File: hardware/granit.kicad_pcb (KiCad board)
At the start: 4 copper layers, 92 x 100 mm, 120 parts, among them J1 USB_C_Receptacle_USB2.0_14P, J2 PCM12SMTR, J3 BM03B-SRSS-TB, J4 SATA_22pin, J5 RJ45_RB1-125B8G1A, J6 12V Screw Terminal, J7 12V Barrel, Q1 2N7002, Q2 FDS4435BZ, Q3 FDS4435BZ, Q4 2N7002, Q5 2N7002, Q6 FDS4435BZ, SW1 SW_Push, U1 USBLC6-2SC6, U2 74AHCT1G125, U3 ASM1061, U4 74AHCT1G32, U5 DS3231MZ, U6 NCP1117-3.3_SOT223, U7 AP64501SP-13, Y1 25MHz

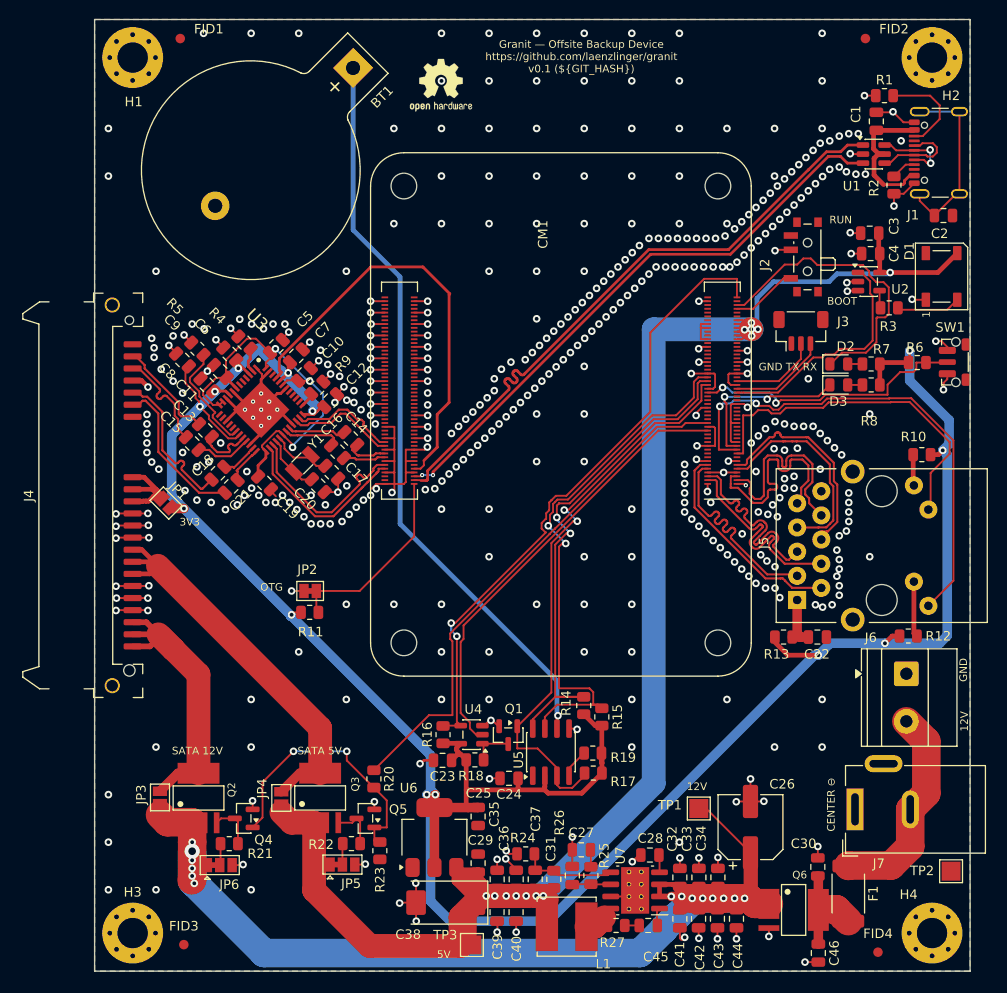
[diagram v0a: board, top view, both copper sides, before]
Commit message: feat: swap RJ45 MagJack to HR911130A (Hanrun GbE)
- New symbol and footprint in granit library
- Pin mapping follows TIA-568B MDI standard
- All 4 Ethernet diff pairs routed with 100Ω impedance
- Pair 1 uses via + bottom trace for length matching
- DRC: 0 violations, 0 unconnected, 0 parity issues
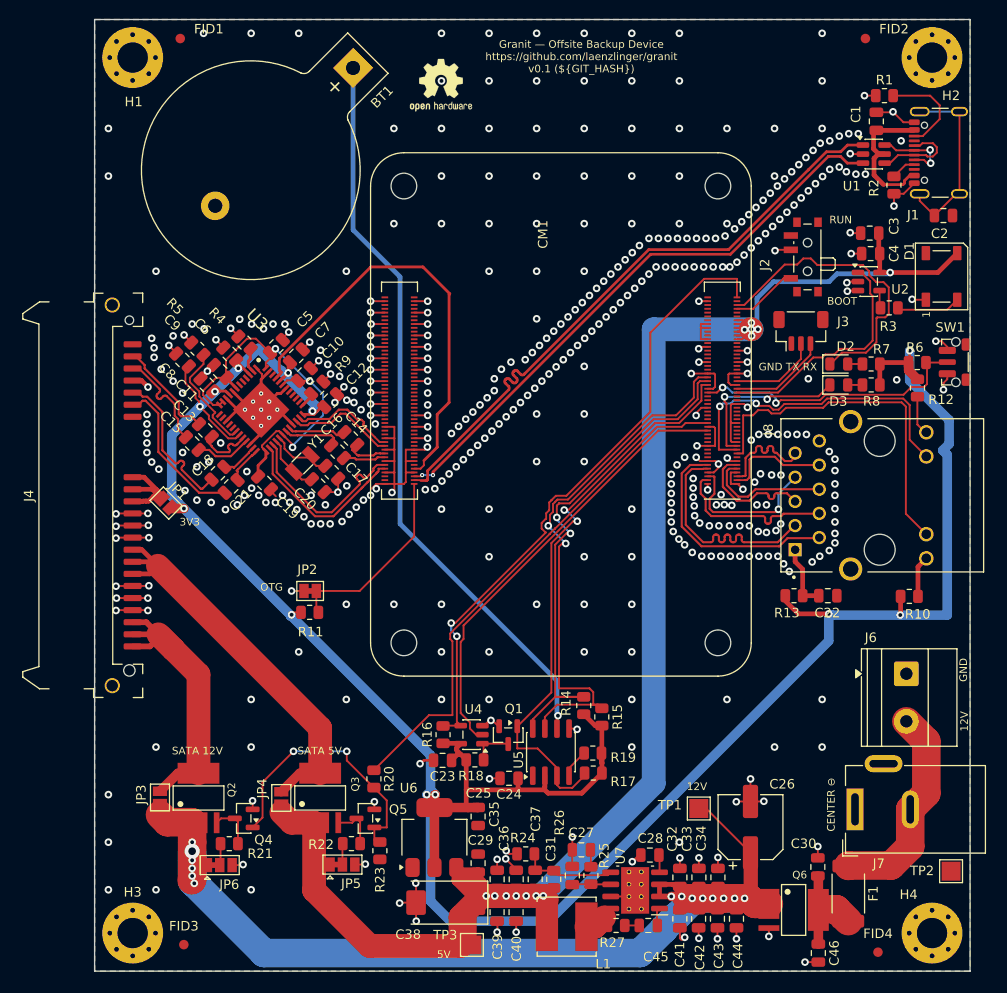
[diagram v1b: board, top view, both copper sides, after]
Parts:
- removed J5: RJ45_RB1-125B8G1A, Connector_RJ:RJ45_UDE_RB1-125B8G1A
- added J8: HR911130A, granit:HANRUN_HR911130A, F.Cu at (102.5, 70.0)
- moved R12 26.1 mm to (106.5, 58.7), turned to -90 degrees
- moved R10 15.0 mm to (105.6, 80.6), turned to 0 degrees
- moved C22 4.48 mm to (97.0, 80.5)
- moved R13 4.48 mm to (93.5, 80.5)
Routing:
- net ETH_nLED1: track 52.5 -> 34.0 mm
- net ETH_P3_N: track 22.2 -> 10.7 mm
- net ETH_P3_P: track 22.3 -> 11.1 mm
- net ETH_P2_P: track 22.6 -> 13.1 mm
- net ETH_P2_N: track 22.3 -> 13.2 mm
- net ETH_P1_N: track 22.2 -> 15.9 mm, vias 0 -> 1
- net ETH_P1_P: track 22.2 -> 17.4 mm
- net Net-(J8-CT_PRI): track 9.85 -> 6.85 mm
- net GND: track 214.3 -> 216.7 mm, vias 450 -> 451
- net ETH_P0_N: track 22.2 -> 24.2 mm
- net ETH_P0_P: track 22.3 -> 24.3 mm
- net Net-(J8-Pad14): track 5.90 -> 4.07 mm
- net Net-(J8-Pad11): track 3.16 -> 4.36 mm
- net +3V3: track 268.9 -> 269.8 mm, vias 13 -> 12

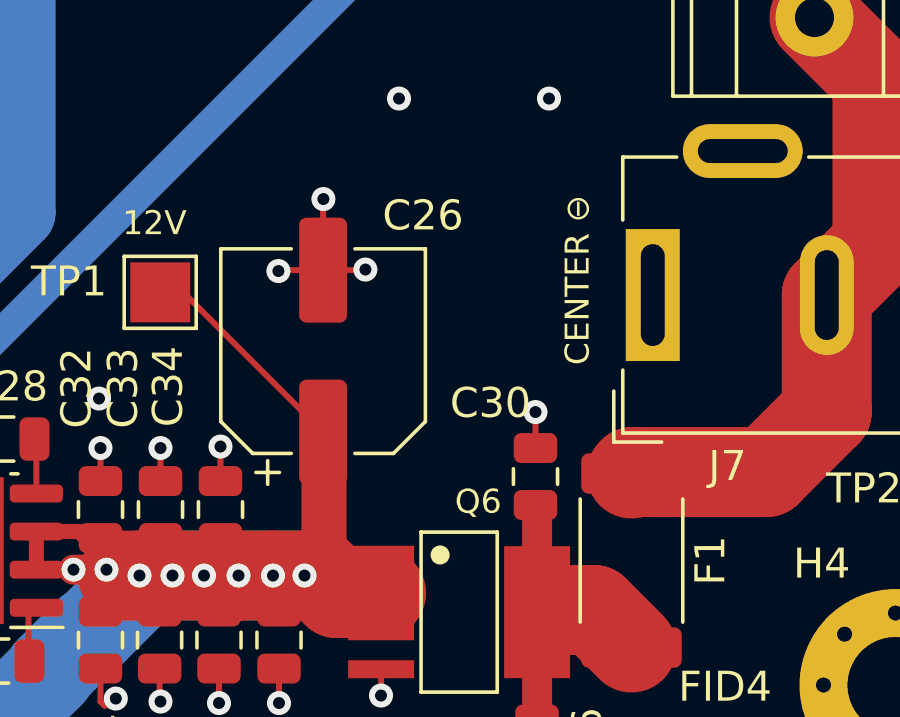
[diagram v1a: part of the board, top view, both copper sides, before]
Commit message: feat: swap C26 footprint to CP_Elec_6.3x7.7 (easier to source on LCSC)
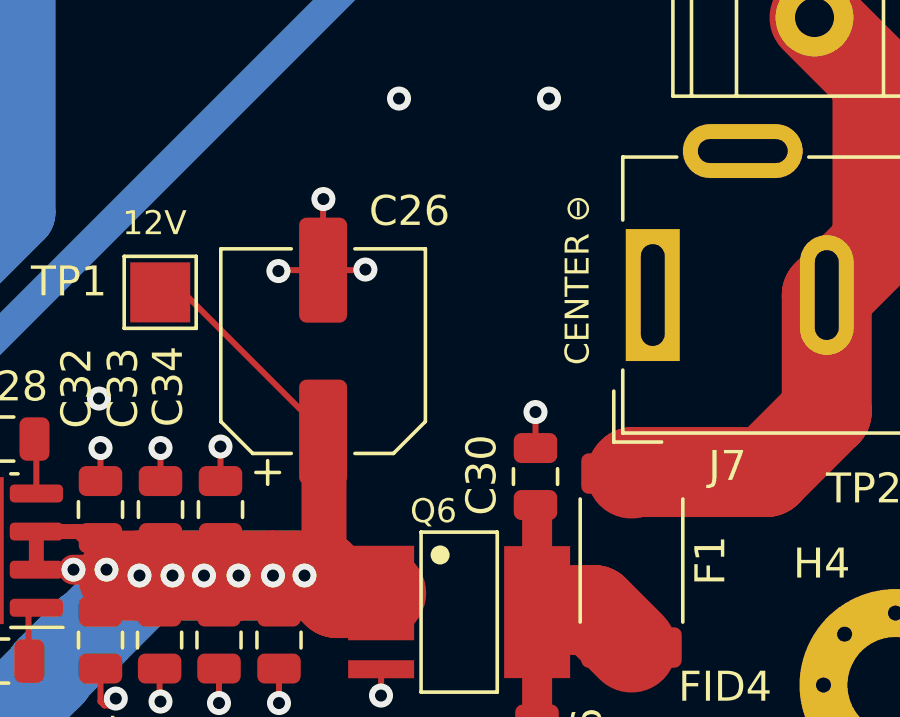
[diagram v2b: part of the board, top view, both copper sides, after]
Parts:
- C26: footprint Capacitor_SMD:CP_Elec_6.3x5.8 -> Capacitor_SMD:CP_Elec_6.3x7.7
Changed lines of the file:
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@@
 		)
 	)
-	(footprint "Capacitor_SMD:CP_Elec_6.3x5.8"
+	(footprint "Capacitor_SMD:CP_Elec_6.3x7.7"
 		(layer "F.Cu")
 		(at 88.92 104.87 90)
-		(descr "SMD capacitor, aluminum electrolytic, Nichicon, 6.3x5.8mm")
+		(descr "SMD capacitor, aluminum electrolytic, Nichicon, 6.3x7.7mm")
 		(tags "capacitor electrolytic")
 		(property "Reference" "C26"
-			(at 4.52 3.33 180)
+			(at 4.67 2.88 180)
 			(layer "F.SilkS")
 			(effects
@@
 		)
 		(property "Value" "100uF/25V"
-			(at 0 4.349999 90)
+			(at 0 4.35 90)
 			(layer "F.Fab")
 			(effects
@@
 		)
 		(embedded_fonts no)
-		(model "${KICAD10_3DMODEL_DIR}/Capacitor_SMD.3dshapes/CP_Elec_6.3x5.8.step"
+		(model "${KICAD10_3DMODEL_DIR}/Capacitor_SMD.3dshapes/CP_Elec_6.3x7.7.step"
 			(offset
 				(xyz 0 0 0)
@@
 		(tags "capacitor")
 		(property "Reference" "C30"
-			(at 2.45 -1.5 180)
+			(at 0.05 -1.8 270)
 			(layer "F.SilkS")
 			(effects
@@
 		(descr "SMALL OUTLINE INTEGRATED CIRCUIT body 3.9 mm/JEDEC MS-012AA (combined pins variation)")
 		(property "Reference" "Q6"
-			(at -3.684205 -0.635205 180)
+			(at -3.369107 0.855255 180)
 			(layer "F.SilkS")
 			(effects

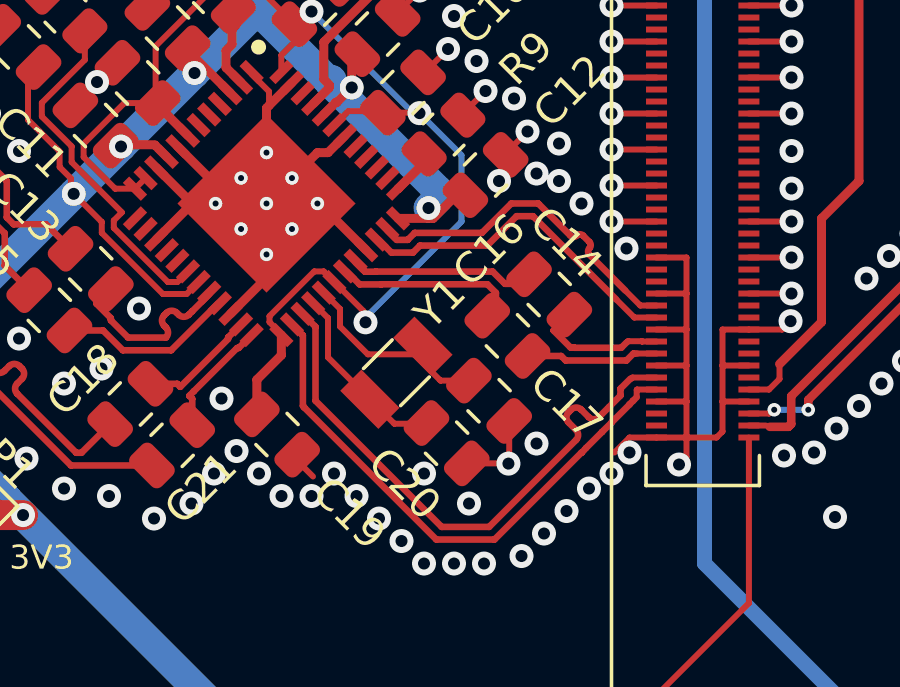
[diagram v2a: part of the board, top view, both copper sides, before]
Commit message: feat: swap crystal Y1 to 2016 4-pin (easier to source)
Changed from Crystal_SMD_3215-2Pin to Crystal_SMD_2016-4Pin_2.0x1.6mm.
Re-routed PCIe area around new crystal placement.
ERC: 0 errors, 0 warnings. DRC: 0 violations.
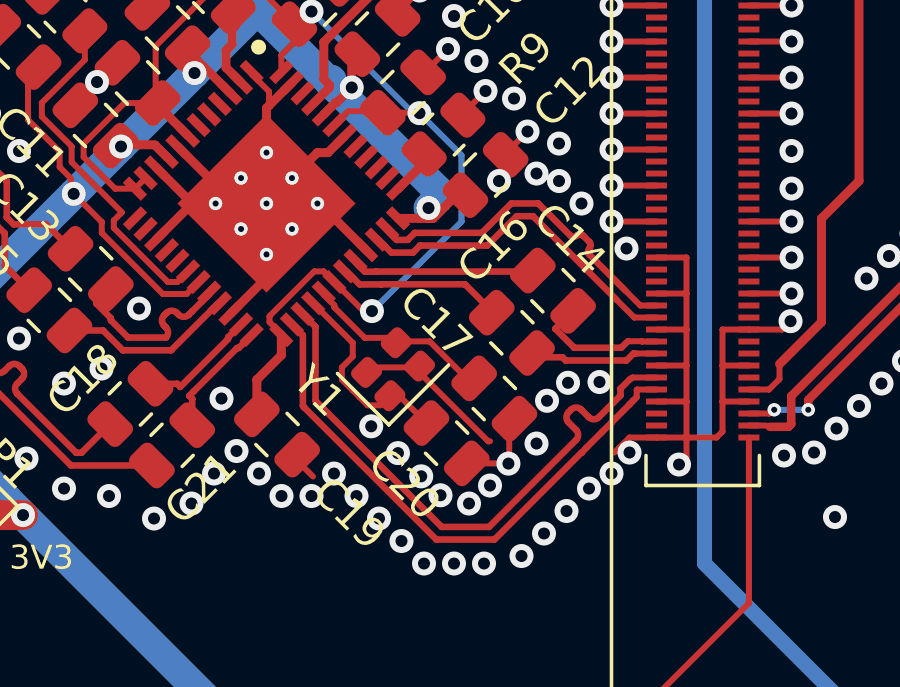
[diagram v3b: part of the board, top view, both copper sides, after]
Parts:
- Y1: footprint Crystal:Crystal_SMD_3215-2Pin_3.2x1.5mm -> Crystal:Crystal_SMD_2016-4Pin_2.0x1.6mm
- moved C17 0.19 mm to (45.1, 67.5)
- moved C16 0.18 mm to (45.7, 65.3)
- moved C14 0.18 mm to (47.0, 63.9)
- moved Y1 0.16 mm to (41.7, 66.5), turned to 45 degrees
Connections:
- Y1 pad 2: Net-(U3-XI) -> GND
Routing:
- net GND: track 216.7 -> 222.1 mm, vias 451 -> 458
- net Net-(U3-XO): track 6.19 -> 7.44 mm

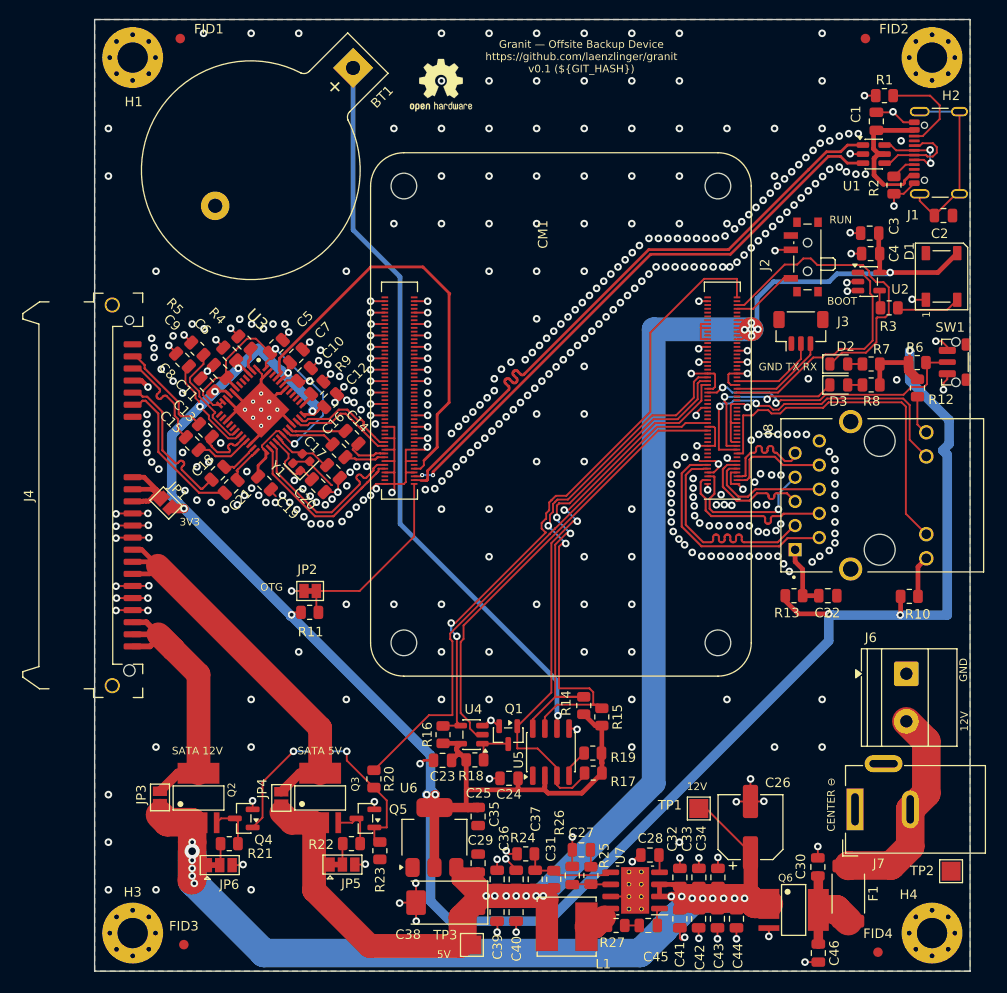
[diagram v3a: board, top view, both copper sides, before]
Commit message: feat: shrink board width to 99.5mm for Hammond 1455 card guide clearance
Board: 92 × 99.5mm (was 92 × 100mm).
Hammond 1455 card guide slot: 100.00 ±0.51mm.
ERC: 0. DRC: 0.
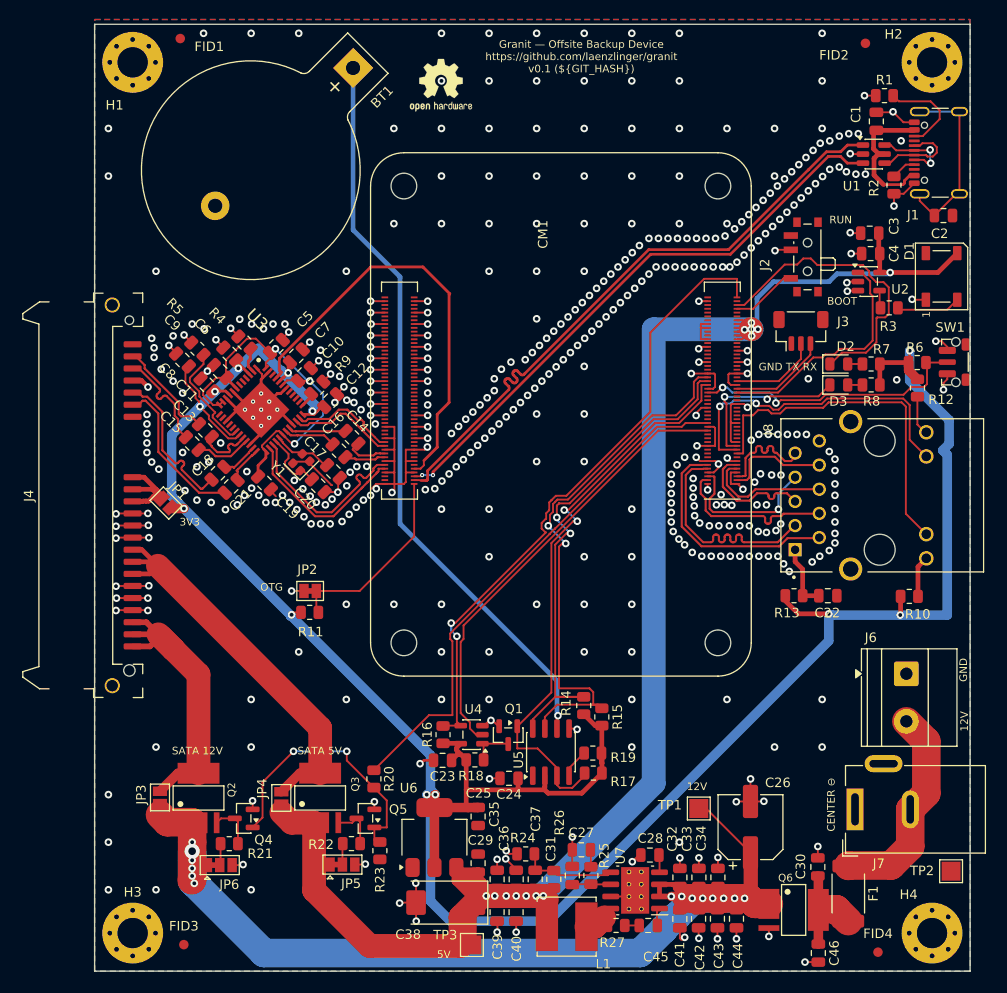
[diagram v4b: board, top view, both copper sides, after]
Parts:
- moved FID2 0.50 mm to (101.0, 22.5)
- moved H1 0.50 mm to (24.0, 24.5)
- moved H2 0.50 mm to (108.0, 24.5)
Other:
- board size 92 x 100 mm -> 92 x 99.5 mm
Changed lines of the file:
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@@
 		(locked yes)
 		(layer "F.Cu")
-		(at 24 24)
+		(at 24 24.5)
 		(descr "Mounting Hole 3.2mm, M3, generated by kicad-footprint-generator mountinghole.py")
 		(tags "mountinghole M3")
 		(property "Reference" "H1"
-			(at 0.1 4.65 0)
+			(at -1.9 4.5 0)
 			(layer "F.SilkS")
 			(effects
@@
 	(footprint "Fiducial:Fiducial_1mm_Mask2mm"
 		(layer "F.Cu")
-		(at 101 22)
+		(at 101 22.5)
 		(descr "Fiducial, circular marking, 1mm bare copper, 2mm soldermask opening (Level A)")
 		(tags "fiducial")
 		(property "Reference" "FID2"
-			(at 3 -1 0)
+			(at -3.3 1.25 0)
 			(layer "F.SilkS")
 			(effects
@@
 		(tags "fiducial")
 		(property "Reference" "FID1"
-			(at 3 -1 0)
+			(at 3.05 0.85 0)
 			(layer "F.SilkS")
 			(effects
@@
 		(locked yes)
 		(layer "F.Cu")
-		(at 108 24)
+		(at 108 24.5)
 		(descr "Mounting Hole 3.2mm, M3, generated by kicad-footprint-generator mountinghole.py")
 		(tags "mountinghole M3")
 		(property "Reference" "H2"
-			(at 2 4 0)
+			(at -4.05 -2.95 0)
 			(layer "F.SilkS")
 			(effects
@@
 	)
 	(gr_rect
-		(start 20 20)
+		(start 20 20.5)
 		(end 112 120)
 		(stroke
 			(width 0.1)
-			(type default)
+			(type solid)
 		)
 		(fill no)
@@
 	)
 	(barcode
-		(at 89.2 25.6 0)
+		(at 89.2 25.8 0)
 		(layer "F.SilkS")
-		(size 9 9)
+		(size 8.5 8.5)
 		(text " https://github.com/laenzlinger/granit")
 		(text_height 1)
@@
 		(layer "Dwgs.User")
 		(pts
-			(xy 112 20) (xy 111.75 47)
-		)
-		(height 11)
-		(orientation 1)
-		(format
-			(prefix "")
-			(suffix "")
-			(units 3)
-			(units_format 0)
-			(precision 4)
-			(suppress_zeroes yes)
-		)
-		(style
-			(thickness 0.1)
-			(arrow_length 1.27)
-			(text_position_mode 0)
-			(arrow_direction outward)
-			(extension_height 0.58642)
-			(extension_offset 0.5)
-			(keep_text_aligned yes)
-		)
-		(gr_text "27"
-			(at 121.85 33.5 90)
-			(layer "Dwgs.User")
-			(effects
-				(font
-					(size 1 1)
-					(thickness 0.15)
-				)
-			)
-		)
-	)
-	(dimension
-		(type orthogonal)
-		(layer "Dwgs.User")
-		(pts
-			(xy 112 20) (xy 110.804 56)
-		)
-		(height 13.55)
-		(orientation 1)
-		(format
-			(prefix "")
-			(suffix "")
-			(units 3)
-			(units_format 0)
-			(precision 4)
-			(suppress_zeroes yes)
-		)
-		(style
-			(thickness 0.1)
-			(arrow_length 1.27)
-			(text_position_mode 0)
-			(arrow_direction outward)
-			(extension_height 0.58642)
-			(extension_offset 0.5)
-			(keep_text_aligned yes)
-		)
-		(gr_text "36"
-			(at 124.4 38 90)
-			(layer "Dwgs.User")
-			(effects
-				(font
-					(size 1 1)
-					(thickness 0.15)
-				)
-			)
-		)
-	)
-	(dimension
-		(type orthogonal)
-		(layer "Dwgs.User")
-		(pts
-			(xy 20 20) (xy 18.95 24)
+			(xy 20 20.5) (xy 18.95 24.5)
 		)
 		(height -4.05)
@@
 		)
 		(gr_text "4"
-			(at 14.8 22 90)
+			(at 14.8 22.5 90)
 			(layer "Dwgs.User")
 			(effects
@@
 		(layer "Dwgs.User")
 		(pts
-			(xy 112 20) (xy 112 120)
+			(xy 112 20.5) (xy 112 120)
 		)
 		(height 25.5)
@@
 			(keep_text_aligned yes)
 		)
-		(gr_text "100"
-			(at 136.35 70 90)
-			(layer "Dwgs.User")
-			(effects
-				(font
-					(size 1 1)
-					(thickness 0.15)
-				)
-			)
-		)
-	)
-	(dimension
-		(type orthogonal)
-		(layer "Dwgs.User")
-		(pts
-			(xy 112 20) (xy 113.609063 103)
-		)
-		(height 20.573005)
-		(orientation 1)
-		(format
-			(prefix "")
-			(suffix "")
-			(units 3)
-			(units_format 0)
-			(precision 4)
-			(suppress_zeroes yes)
-		)
-		(style
-			(thickness 0.1)
-			(arrow_length 1.27)
-			(text_position_mode 0)
-			(arrow_direction outward)
-			(extension_height 0.58642)
-			(extension_offset 0.5)
-			(keep_text_aligned yes)
-		)
-		(gr_text "83"
-			(at 131.423005 61.5 90)
-			(layer "Dwgs.User")
-			(effects
-				(font
-					(size 1 1)
-					(thickness 0.15)
-				)
-			)
-		)
-	)
-	(dimension
-		(type orthogonal)
-		(layer "Dwgs.User")
-		(pts
-			(xy 112 20) (xy 112.4 34)
-		)
-		(height 8)
-		(orientation 1)
-		(format
-			(prefix "")
-			(suffix "")
-			(units 3)
-			(units_format 0)
-			(precision 4)
-			(suppress_zeroes yes)
-		)
-		(style
-			(thickness 0.1)
-			(arrow_length 1.27)
-			(text_position_mode 0)
-			(arrow_direction outward)
-			(extension_height 0.58642)
-			(extension_offset 0.5)
-			(keep_text_aligned yes)
-		)
-		(gr_text "14"
-			(at 118.85 27 90)
+		(gr_text "99.5"
+			(at 136.35 70.25 90)
 			(layer "Dwgs.User")
 			(effects
@@
 	)
 	(segment
-		(start 107.019594 32.25)
-		(end 108.8 30.469594)
+		(start 107.85 28.6)
+		(end 104.5125 28.6)
 		(width 0.2)
 		(layer "F.Cu")
@@
 	)
 	(segment
-		(start 108.8 29)
-		(end 107.8 28)
+		(start 106.13 32.25)
+		(end 107.019594 32.25)
 		(width 0.2)
 		(layer "F.Cu")
@@
 	)
 	(segment
-		(start 108.8 30.469594)
-		(end 108.8 29)
+		(start 107.019594 32.25)
+		(end 108.8 30.469594)
 		(width 0.2)
 		(layer "F.Cu")
@@
 	)
 	(segment
-		(start 107.8 28)
-		(end 103.9125 28)
+		(start 108.8 29.55)
+		(end 107.85 28.6)
 		(width 0.2)
 		(layer "F.Cu")
@@
 	)
 	(segment
-		(start 106.13 32.25)
-		(end 107.019594 32.25)
+		(start 108.8 30.469594)
+		(end 108.8 29.55)
+		(width 0.2)
+		(layer "F.Cu")
+		(net "Net-(J1-CC2)")
+	)
+	(segment
+		(start 104.5125 28.6)
+		(end 103.9125 28)
 		(width 0.2)
 		(layer "F.Cu")
